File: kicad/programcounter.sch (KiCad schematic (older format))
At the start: 6 parts, among them U20 74LS161, U21 74LS245

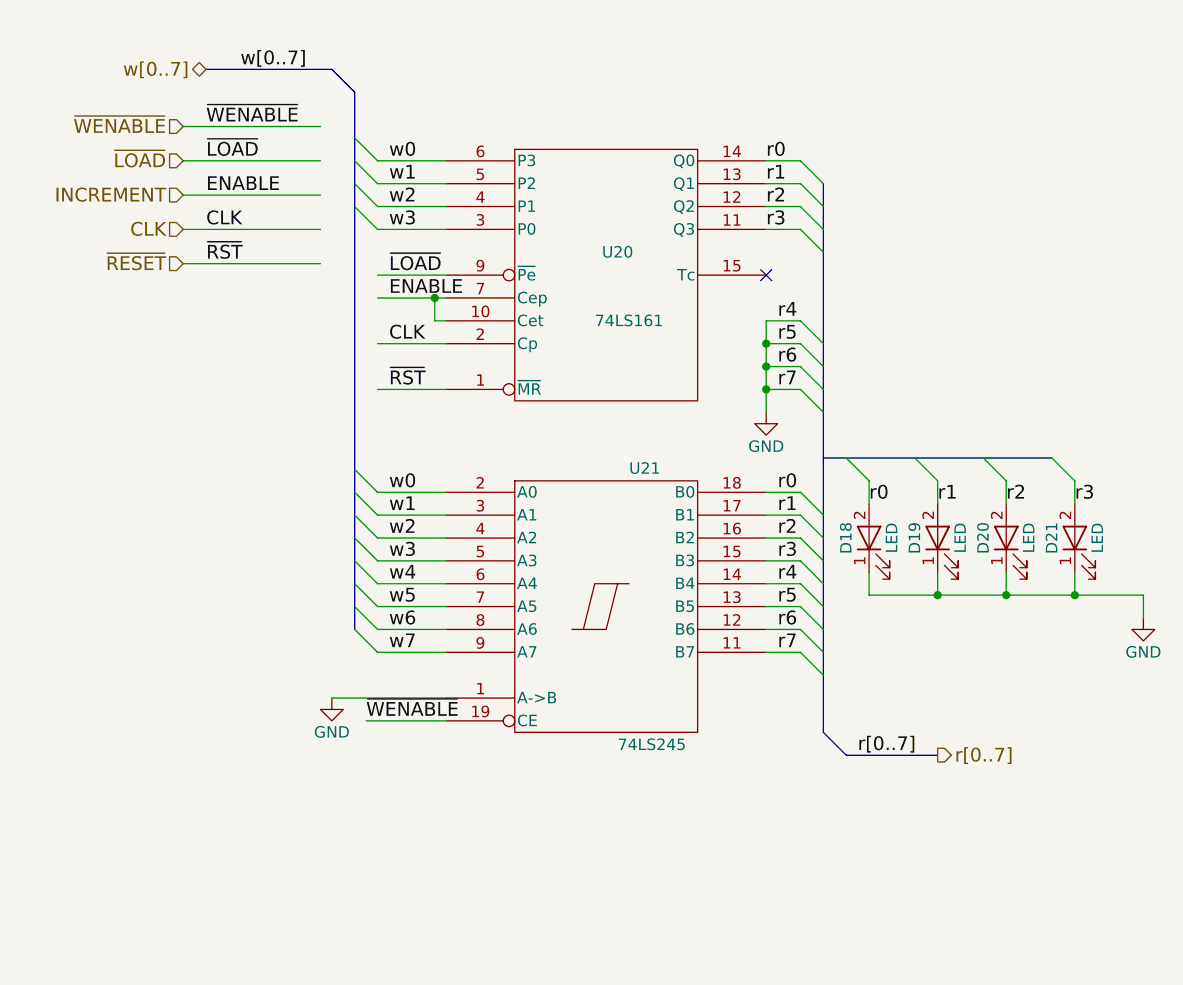
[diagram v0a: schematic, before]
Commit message: Update bugfix version to use updated kicad libraries
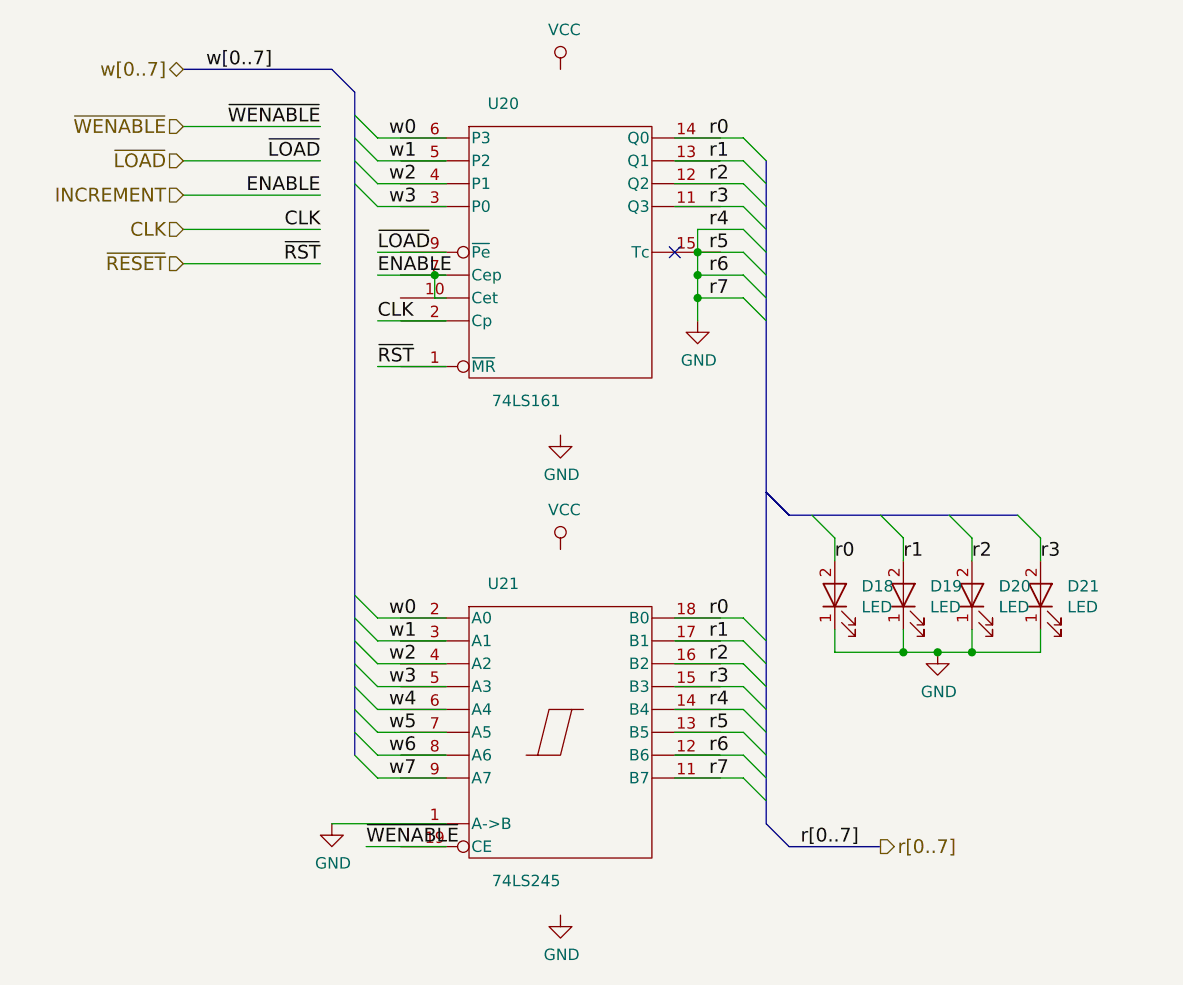
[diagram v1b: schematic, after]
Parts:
- removed D18, D19, D20, D21: LED, LEDs:LED-5MM, symbol LED
- removed U20: 74LS161, Housings_DIP:DIP-16_W7.62mm_LongPads, symbol 74LS161
- removed U21: 74LS245, Housings_DIP:DIP-20_W7.62mm_LongPads, symbol 74LS245
- added D18, D19, D20, D21: LED, symbol Device:LED
- added U20: 74LS161, symbol 74xx:74LS161
- added U21: 74LS245, symbol 74xx:74LS245
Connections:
- net labels added: VCC
- wire segments 52 -> 58
